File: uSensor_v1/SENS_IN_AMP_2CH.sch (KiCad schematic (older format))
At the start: 19 parts, among them U16 TBD

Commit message: Layout correction in progress.
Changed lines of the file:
@@
 AR Path="/5CFE311F/5C6F0205" Ref="R52"  Part="1"
 AR Path="/5E594B34/5C6F0205" Ref="R60"  Part="1"
-F 0 "R52" V 2443 3950 50  0000 C CNN
+F 0 "R60" V 2443 3950 50  0000 C CNN
 F 1 "10k 1%" V 2534 3950 50  0000 C CNN
 F 2 "Resistor_SMD:R_0603_1608Metric_Pad1.05x0.95mm_HandSolder" V 2580 3950 50  0001 C CNN
@@
 AR Path="/5CFE311F/5C6F020C" Ref="C49"  Part="1"
 AR Path="/5E594B34/5C6F020C" Ref="C53"  Part="1"
-F 0 "C49" V 3298 2800 50  0000 C CNN
+F 0 "C53" V 3298 2800 50  0000 C CNN
 F 1 "1p 16V X5R" V 3389 2800 50  0000 C CNN
 F 2 "Capacitor_SMD:C_0603_1608Metric_Pad1.05x0.95mm_HandSolder" H 3588 2650 50  0001 C CNN
@@
 AR Path="/5CFE311F/5C6F0213" Ref="R54"  Part="1"
 AR Path="/5E594B34/5C6F0213" Ref="R62"  Part="1"
-F 0 "R54" H 2830 4154 50  0000 R CNN
+F 0 "R62" H 2830 4154 50  0000 R CNN
 F 1 "22k 1%" H 2830 4245 50  0000 R CNN
 F 2 "Resistor_SMD:R_0603_1608Metric_Pad1.05x0.95mm_HandSolder" V 2830 4200 50  0001 C CNN
@@
 AR Path="/5CFE311F/5C6F0221" Ref="R36"  Part="1"
 AR Path="/5E594B34/5C6F0221" Ref="R58"  Part="1"
-F 0 "R36" V 2443 3600 50  0000 C CNN
+F 0 "R58" V 2443 3600 50  0000 C CNN
 F 1 "10k 1%" V 2534 3600 50  0000 C CNN
 F 2 "Resistor_SMD:R_0603_1608Metric_Pad1.05x0.95mm_HandSolder" V 2580 3600 50  0001 C CNN
@@
 AR Path="/5CFE311F/5C6F0228" Ref="R34"  Part="1"
 AR Path="/5E594B34/5C6F0228" Ref="R56"  Part="1"
-F 0 "R34" V 3343 3150 50  0000 C CNN
+F 0 "R56" V 3343 3150 50  0000 C CNN
 F 1 "22k 1%" V 3434 3150 50  0000 C CNN
 F 2 "Resistor_SMD:R_0603_1608Metric_Pad1.05x0.95mm_HandSolder" V 3480 3150 50  0001 C CNN
@@
 AR Path="/5CFE311F/5D2C6388" Ref="TP61"  Part="1"
 AR Path="/5E594B34/5D2C6388" Ref="TP65"  Part="1"
-F 0 "TP61" H 3100 3225 50  0000 C CNN
+F 0 "TP65" H 3100 3225 50  0000 C CNN
 F 1 "TP" H 3100 3134 50  0000 C CNN
 F 2 "Sentisa-Connectors:TestPoint_Probe_1.0mmDiameter_0.6mmDrill" H 3300 2900 50  0001 C CNN
@@
 AR Path="/5CFE311F/5D2C69C6" Ref="TP63"  Part="1"
 AR Path="/5E594B34/5D2C69C6" Ref="TP67"  Part="1"
-F 0 "TP63" H 3200 3975 50  0000 C CNN
+F 0 "TP67" H 3200 3975 50  0000 C CNN
 F 1 "TP" H 3200 3884 50  0000 C CNN
 F 2 "Sentisa-Connectors:TestPoint_Probe_1.0mmDiameter_0.6mmDrill" H 3400 3650 50  0001 C CNN
@@
 AR Path="/5CFE311F/5D1D3C08" Ref="R53"  Part="1"
 AR Path="/5E594B34/5D1D3C08" Ref="R61"  Part="1"
-F 0 "R53" V 5743 3950 50  0000 C CNN
+F 0 "R61" V 5743 3950 50  0000 C CNN
 F 1 "10k 1%" V 5834 3950 50  0000 C CNN
 F 2 "Resistor_SMD:R_0603_1608Metric_Pad1.05x0.95mm_HandSolder" V 5880 3950 50  0001 C CNN
@@
 AR Path="/5CFE311F/5D1D3C0F" Ref="C50"  Part="1"
 AR Path="/5E594B34/5D1D3C0F" Ref="C55"  Part="1"
-F 0 "C50" V 6598 2800 50  0000 C CNN
+F 0 "C55" V 6598 2800 50  0000 C CNN
 F 1 "1p 16V X5R" V 6689 2800 50  0000 C CNN
 F 2 "Capacitor_SMD:C_0603_1608Metric_Pad1.05x0.95mm_HandSolder" H 6888 2650 50  0001 C CNN
@@
 AR Path="/5CFE311F/5D1D3C16" Ref="R55"  Part="1"
 AR Path="/5E594B34/5D1D3C16" Ref="R63"  Part="1"
-F 0 "R55" H 6130 4154 50  0000 R CNN
+F 0 "R63" H 6130 4154 50  0000 R CNN
 F 1 "22k 1%" H 6130 4245 50  0000 R CNN
 F 2 "Resistor_SMD:R_0603_1608Metric_Pad1.05x0.95mm_HandSolder" V 6130 4200 50  0001 C CNN
@@
 AR Path="/5CFE311F/5D1D3C22" Ref="R37"  Part="1"
 AR Path="/5E594B34/5D1D3C22" Ref="R59"  Part="1"
-F 0 "R37" V 5743 3600 50  0000 C CNN
+F 0 "R59" V 5743 3600 50  0000 C CNN
 F 1 "10k 1%" V 5834 3600 50  0000 C CNN
 F 2 "Resistor_SMD:R_0603_1608Metric_Pad1.05x0.95mm_HandSolder" V 5880 3600 50  0001 C CNN
@@
 AR Path="/5CFE311F/5D1D3C29" Ref="R35"  Part="1"
 AR Path="/5E594B34/5D1D3C29" Ref="R57"  Part="1"
-F 0 "R35" V 6643 3150 50  0000 C CNN
+F 0 "R57" V 6643 3150 50  0000 C CNN
 F 1 "22k 1%" V 6734 3150 50  0000 C CNN
 F 2 "Resistor_SMD:R_0603_1608Metric_Pad1.05x0.95mm_HandSolder" V 6780 3150 50  0001 C CNN
@@
 AR Path="/5CFE311F/5D1D3C38" Ref="C51"  Part="1"
 AR Path="/5E594B34/5D1D3C38" Ref="C56"  Part="1"
-F 0 "C51" H 9215 3296 50  0000 L CNN
+F 0 "C56" H 9215 3296 50  0000 L CNN
 F 1 "100n 6V3 X5R" H 9215 3205 50  0000 L CNN
 F 2 "Capacitor_SMD:C_0603_1608Metric_Pad1.05x0.95mm_HandSolder" H 9138 3100 50  0001 C CNN
@@
 AR Path="/5CFE311F/5D1D3C3F" Ref="C52"  Part="1"
 AR Path="/5E594B34/5D1D3C3F" Ref="C58"  Part="1"
-F 0 "C52" H 9215 4546 50  0000 L CNN
+F 0 "C58" H 9215 4546 50  0000 L CNN
 F 1 "100n 6V3 X5R" H 9215 4455 50  0000 L CNN
 F 2 "Capacitor_SMD:C_0603_1608Metric_Pad1.05x0.95mm_HandSolder" H 9138 4350 50  0001 C CNN
@@
 AR Path="/5CFE311F/5D1D3C6C" Ref="TP62"  Part="1"
 AR Path="/5E594B34/5D1D3C6C" Ref="TP66"  Part="1"
-F 0 "TP62" H 6400 3225 50  0000 C CNN
+F 0 "TP66" H 6400 3225 50  0000 C CNN
 F 1 "TP" H 6400 3134 50  0000 C CNN
 F 2 "Sentisa-Connectors:TestPoint_Probe_1.0mmDiameter_0.6mmDrill" H 6600 2900 50  0001 C CNN
@@
 AR Path="/5CFE311F/5D1D3C73" Ref="TP64"  Part="1"
 AR Path="/5E594B34/5D1D3C73" Ref="TP68"  Part="1"
-F 0 "TP64" H 6500 3975 50  0000 C CNN
+F 0 "TP68" H 6500 3975 50  0000 C CNN
 F 1 "TP" H 6500 3884 50  0000 C CNN
 F 2 "Sentisa-Connectors:TestPoint_Probe_1.0mmDiameter_0.6mmDrill" H 6700 3650 50  0001 C CNN
@@
 AR Path="/5CFE311F/5F717FB4" Ref="U16"  Part="1"
 AR Path="/5E594B34/5F717FB4" Ref="U17"  Part="1"
-F 0 "U16" H 3600 4217 50  0000 C CNN
+F 0 "U17" H 3600 4217 50  0000 C CNN
 F 1 "TBD" H 3600 4126 50  0000 C CNN
 F 2 "Sentisa-IC:SO-8" H 3600 3850 50  0001 C CNN
@@
 AR Path="/5CFE311F/5F718017" Ref="U16"  Part="2"
 AR Path="/5E594B34/5F718017" Ref="U17"  Part="2"
-F 0 "U16" H 6900 4217 50  0000 C CNN
+F 0 "U17" H 6900 4217 50  0000 C CNN
 F 1 "TBD" H 6900 4126 50  0000 C CNN
 F 2 "Sentisa-IC:SO-8" H 6900 3850 50  0001 C CNN
@@
 AR Path="/5CFE311F/5F7180AE" Ref="U16"  Part="3"
 AR Path="/5E594B34/5F7180AE" Ref="U17"  Part="3"
-F 0 "U16" H 8808 3646 50  0000 L CNN
+F 0 "U17" H 8808 3646 50  0000 L CNN
 F 1 "TBD" H 8808 3555 50  0000 L CNN
 F 2 "Sentisa-IC:SO-8" H 8850 3600 50  0001 C CNN
@@
 AR Path="/5E594B34/5D0CECC5" Ref="C60"  Part="1"
 AR Path="/5CFE311F/5D0CECC5" Ref="C48"  Part="1"
-F 0 "C48" H 5585 4246 50  0000 R CNN
+F 0 "C60" H 5585 4246 50  0000 R CNN
 F 1 "10n 6V3 X5R" H 5585 4155 50  0000 R CNN
 F 2 "Capacitor_SMD:C_0603_1608Metric_Pad1.05x0.95mm_HandSolder" H 5738 4050 50  0001 C CNN
@@
 AR Path="/5E594B34/5D0D3A39" Ref="C59"  Part="1"
 AR Path="/5CFE311F/5D0D3A39" Ref="C44"  Part="1"
-F 0 "C44" H 2285 4246 50  0000 R CNN
+F 0 "C59" H 2285 4246 50  0000 R CNN
 F 1 "10n 6V3 X5R" H 2285 4155 50  0000 R CNN
 F 2 "Capacitor_SMD:C_0603_1608Metric_Pad1.05x0.95mm_HandSolder" H 2438 4050 50  0001 C CNN

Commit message: Components checked.
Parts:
- U16: value TBD -> MCP6H02-E/SN; MFR TBD -> Microchip; MPN TBD -> MCP6H02-E/SN
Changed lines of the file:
@@
 AR Path="/5CFE311F/5C6F0205" Ref="R52"  Part="1"
 AR Path="/5E594B34/5C6F0205" Ref="R60"  Part="1"
-F 0 "R60" V 2443 3950 50  0000 C CNN
+F 0 "R52" V 2443 3950 50  0000 C CNN
 F 1 "10k 1%" V 2534 3950 50  0000 C CNN
 F 2 "Resistor_SMD:R_0603_1608Metric_Pad1.05x0.95mm_HandSolder" V 2580 3950 50  0001 C CNN
@@
 AR Path="/5CFE311F/5C6F020C" Ref="C49"  Part="1"
 AR Path="/5E594B34/5C6F020C" Ref="C53"  Part="1"
-F 0 "C53" V 3298 2800 50  0000 C CNN
+F 0 "C49" V 3298 2800 50  0000 C CNN
 F 1 "1p 16V X5R" V 3389 2800 50  0000 C CNN
 F 2 "Capacitor_SMD:C_0603_1608Metric_Pad1.05x0.95mm_HandSolder" H 3588 2650 50  0001 C CNN
@@
 AR Path="/5CFE311F/5C6F0213" Ref="R54"  Part="1"
 AR Path="/5E594B34/5C6F0213" Ref="R62"  Part="1"
-F 0 "R62" H 2830 4154 50  0000 R CNN
+F 0 "R54" H 2830 4154 50  0000 R CNN
 F 1 "22k 1%" H 2830 4245 50  0000 R CNN
 F 2 "Resistor_SMD:R_0603_1608Metric_Pad1.05x0.95mm_HandSolder" V 2830 4200 50  0001 C CNN
@@
 AR Path="/5CFE311F/5C6F0221" Ref="R36"  Part="1"
 AR Path="/5E594B34/5C6F0221" Ref="R58"  Part="1"
-F 0 "R58" V 2443 3600 50  0000 C CNN
+F 0 "R36" V 2443 3600 50  0000 C CNN
 F 1 "10k 1%" V 2534 3600 50  0000 C CNN
 F 2 "Resistor_SMD:R_0603_1608Metric_Pad1.05x0.95mm_HandSolder" V 2580 3600 50  0001 C CNN
@@
 AR Path="/5CFE311F/5C6F0228" Ref="R34"  Part="1"
 AR Path="/5E594B34/5C6F0228" Ref="R56"  Part="1"
-F 0 "R56" V 3343 3150 50  0000 C CNN
+F 0 "R34" V 3343 3150 50  0000 C CNN
 F 1 "22k 1%" V 3434 3150 50  0000 C CNN
 F 2 "Resistor_SMD:R_0603_1608Metric_Pad1.05x0.95mm_HandSolder" V 3480 3150 50  0001 C CNN
@@
 AR Path="/5CFE311F/5D2C6388" Ref="TP61"  Part="1"
 AR Path="/5E594B34/5D2C6388" Ref="TP65"  Part="1"
-F 0 "TP65" H 3100 3225 50  0000 C CNN
+F 0 "TP61" H 3100 3225 50  0000 C CNN
 F 1 "TP" H 3100 3134 50  0000 C CNN
 F 2 "Sentisa-Connectors:TestPoint_Probe_1.0mmDiameter_0.6mmDrill" H 3300 2900 50  0001 C CNN
@@
 AR Path="/5CFE311F/5D2C69C6" Ref="TP63"  Part="1"
 AR Path="/5E594B34/5D2C69C6" Ref="TP67"  Part="1"
-F 0 "TP67" H 3200 3975 50  0000 C CNN
+F 0 "TP63" H 3200 3975 50  0000 C CNN
 F 1 "TP" H 3200 3884 50  0000 C CNN
 F 2 "Sentisa-Connectors:TestPoint_Probe_1.0mmDiameter_0.6mmDrill" H 3400 3650 50  0001 C CNN
@@
 AR Path="/5CFE311F/5D1D3C08" Ref="R53"  Part="1"
 AR Path="/5E594B34/5D1D3C08" Ref="R61"  Part="1"
-F 0 "R61" V 5743 3950 50  0000 C CNN
+F 0 "R53" V 5743 3950 50  0000 C CNN
 F 1 "10k 1%" V 5834 3950 50  0000 C CNN
 F 2 "Resistor_SMD:R_0603_1608Metric_Pad1.05x0.95mm_HandSolder" V 5880 3950 50  0001 C CNN
@@
 AR Path="/5CFE311F/5D1D3C0F" Ref="C50"  Part="1"
 AR Path="/5E594B34/5D1D3C0F" Ref="C55"  Part="1"
-F 0 "C55" V 6598 2800 50  0000 C CNN
+F 0 "C50" V 6598 2800 50  0000 C CNN
 F 1 "1p 16V X5R" V 6689 2800 50  0000 C CNN
 F 2 "Capacitor_SMD:C_0603_1608Metric_Pad1.05x0.95mm_HandSolder" H 6888 2650 50  0001 C CNN
@@
 AR Path="/5CFE311F/5D1D3C16" Ref="R55"  Part="1"
 AR Path="/5E594B34/5D1D3C16" Ref="R63"  Part="1"
-F 0 "R63" H 6130 4154 50  0000 R CNN
+F 0 "R55" H 6130 4154 50  0000 R CNN
 F 1 "22k 1%" H 6130 4245 50  0000 R CNN
 F 2 "Resistor_SMD:R_0603_1608Metric_Pad1.05x0.95mm_HandSolder" V 6130 4200 50  0001 C CNN
@@
 AR Path="/5CFE311F/5D1D3C22" Ref="R37"  Part="1"
 AR Path="/5E594B34/5D1D3C22" Ref="R59"  Part="1"
-F 0 "R59" V 5743 3600 50  0000 C CNN
+F 0 "R37" V 5743 3600 50  0000 C CNN
 F 1 "10k 1%" V 5834 3600 50  0000 C CNN
 F 2 "Resistor_SMD:R_0603_1608Metric_Pad1.05x0.95mm_HandSolder" V 5880 3600 50  0001 C CNN
@@
 AR Path="/5CFE311F/5D1D3C29" Ref="R35"  Part="1"
 AR Path="/5E594B34/5D1D3C29" Ref="R57"  Part="1"
-F 0 "R57" V 6643 3150 50  0000 C CNN
+F 0 "R35" V 6643 3150 50  0000 C CNN
 F 1 "22k 1%" V 6734 3150 50  0000 C CNN
 F 2 "Resistor_SMD:R_0603_1608Metric_Pad1.05x0.95mm_HandSolder" V 6780 3150 50  0001 C CNN
@@
 AR Path="/5CFE311F/5D1D3C38" Ref="C51"  Part="1"
 AR Path="/5E594B34/5D1D3C38" Ref="C56"  Part="1"
-F 0 "C56" H 9215 3296 50  0000 L CNN
+F 0 "C51" H 9215 3296 50  0000 L CNN
 F 1 "100n 6V3 X5R" H 9215 3205 50  0000 L CNN
 F 2 "Capacitor_SMD:C_0603_1608Metric_Pad1.05x0.95mm_HandSolder" H 9138 3100 50  0001 C CNN
@@
 AR Path="/5CFE311F/5D1D3C3F" Ref="C52"  Part="1"
 AR Path="/5E594B34/5D1D3C3F" Ref="C58"  Part="1"
-F 0 "C58" H 9215 4546 50  0000 L CNN
+F 0 "C52" H 9215 4546 50  0000 L CNN
 F 1 "100n 6V3 X5R" H 9215 4455 50  0000 L CNN
 F 2 "Capacitor_SMD:C_0603_1608Metric_Pad1.05x0.95mm_HandSolder" H 9138 4350 50  0001 C CNN
@@
 AR Path="/5CFE311F/5D1D3C6C" Ref="TP62"  Part="1"
 AR Path="/5E594B34/5D1D3C6C" Ref="TP66"  Part="1"
-F 0 "TP66" H 6400 3225 50  0000 C CNN
+F 0 "TP62" H 6400 3225 50  0000 C CNN
 F 1 "TP" H 6400 3134 50  0000 C CNN
 F 2 "Sentisa-Connectors:TestPoint_Probe_1.0mmDiameter_0.6mmDrill" H 6600 2900 50  0001 C CNN
@@
 AR Path="/5CFE311F/5D1D3C73" Ref="TP64"  Part="1"
 AR Path="/5E594B34/5D1D3C73" Ref="TP68"  Part="1"
-F 0 "TP68" H 6500 3975 50  0000 C CNN
+F 0 "TP64" H 6500 3975 50  0000 C CNN
 F 1 "TP" H 6500 3884 50  0000 C CNN
 F 2 "Sentisa-Connectors:TestPoint_Probe_1.0mmDiameter_0.6mmDrill" H 6700 3650 50  0001 C CNN
@@
 AR Path="/5CFE311F/5F717FB4" Ref="U16"  Part="1"
 AR Path="/5E594B34/5F717FB4" Ref="U17"  Part="1"
-F 0 "U17" H 3600 4217 50  0000 C CNN
-F 1 "TBD" H 3600 4126 50  0000 C CNN
+F 0 "U16" H 3600 4217 50  0000 C CNN
+F 1 "MCP6H02-E/SN" H 3600 4126 50  0000 C CNN
 F 2 "Sentisa-IC:SO-8" H 3600 3850 50  0001 C CNN
 F 3 "" H 3600 3850 50  0001 C CNN
-F 4 "TBD" H 3600 3850 50  0001 C CNN "MFR"
-F 5 "TBD" H 3600 3850 50  0001 C CNN "MPN"
+F 4 "Microchip" H 3600 3850 50  0001 C CNN "MFR"
+F 5 "MCP6H02-E/SN" H 3600 3850 50  0001 C CNN "MPN"
 	1    3600 3850
 	1    0    0    -1
@@
 AR Path="/5CFE311F/5F718017" Ref="U16"  Part="2"
 AR Path="/5E594B34/5F718017" Ref="U17"  Part="2"
-F 0 "U17" H 6900 4217 50  0000 C CNN
-F 1 "TBD" H 6900 4126 50  0000 C CNN
+F 0 "U16" H 6900 4217 50  0000 C CNN
+F 1 "MCP6H02-E/SN" H 6900 4126 50  0000 C CNN
 F 2 "Sentisa-IC:SO-8" H 6900 3850 50  0001 C CNN
 F 3 "" H 6900 3850 50  0001 C CNN
-F 4 "TBD" H 6900 3850 50  0001 C CNN "MFR"
-F 5 "TBD" H 6900 3850 50  0001 C CNN "MPN"
+F 4 "Microchip" H 6900 3850 50  0001 C CNN "MFR"
+F 5 "MCP6H02-E/SN" H 6900 3850 50  0001 C CNN "MPN"
 	2    6900 3850
 	1    0    0    -1
@@
 AR Path="/5CFE311F/5F7180AE" Ref="U16"  Part="3"
 AR Path="/5E594B34/5F7180AE" Ref="U17"  Part="3"
-F 0 "U17" H 8808 3646 50  0000 L CNN
+F 0 "U16" H 8808 3646 50  0000 L CNN
 F 1 "TBD" H 8808 3555 50  0000 L CNN
 F 2 "Sentisa-IC:SO-8" H 8850 3600 50  0001 C CNN
@@
 AR Path="/5E594B34/5D0CECC5" Ref="C60"  Part="1"
 AR Path="/5CFE311F/5D0CECC5" Ref="C48"  Part="1"
-F 0 "C60" H 5585 4246 50  0000 R CNN
+F 0 "C48" H 5585 4246 50  0000 R CNN
 F 1 "10n 6V3 X5R" H 5585 4155 50  0000 R CNN
 F 2 "Capacitor_SMD:C_0603_1608Metric_Pad1.05x0.95mm_HandSolder" H 5738 4050 50  0001 C CNN
@@
 AR Path="/5E594B34/5D0D3A39" Ref="C59"  Part="1"
 AR Path="/5CFE311F/5D0D3A39" Ref="C44"  Part="1"
-F 0 "C59" H 2285 4246 50  0000 R CNN
+F 0 "C44" H 2285 4246 50  0000 R CNN
 F 1 "10n 6V3 X5R" H 2285 4155 50  0000 R CNN
 F 2 "Capacitor_SMD:C_0603_1608Metric_Pad1.05x0.95mm_HandSolder" H 2438 4050 50  0001 C CNN

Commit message: Layout in progress (adding vias)
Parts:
- U16: value TBD -> MCP6H02-E/SN; MFR TBD -> Microchip; MPN TBD -> MCP6H02-E/SN
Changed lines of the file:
@@
 AR Path="/5E594B34/5F7180AE" Ref="U17"  Part="3"
 F 0 "U16" H 8808 3646 50  0000 L CNN
-F 1 "TBD" H 8808 3555 50  0000 L CNN
+F 1 "MCP6H02-E/SN" H 8808 3555 50  0000 L CNN
 F 2 "Sentisa-IC:SO-8" H 8850 3600 50  0001 C CNN
 F 3 "" H 8850 3600 50  0001 C CNN
-F 4 "TBD" H 8850 3600 50  0001 C CNN "MFR"
-F 5 "TBD" H 8850 3600 50  0001 C CNN "MPN"
+F 4 "Microchip" H 8850 3600 50  0001 C CNN "MFR"
+F 5 "MCP6H02-E/SN" H 8850 3600 50  0001 C CNN "MPN"
 	3    8850 3600
 	1    0    0    -1

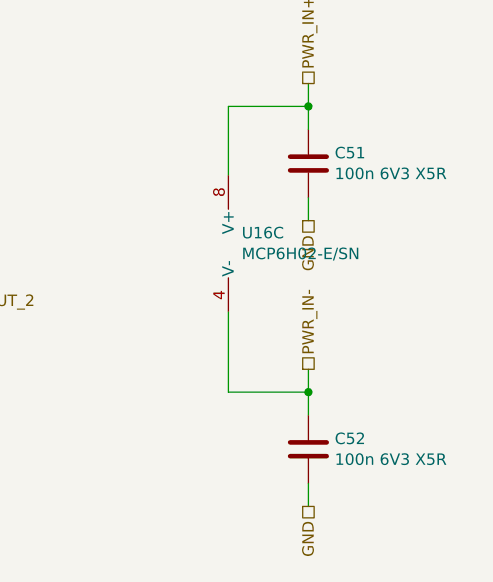
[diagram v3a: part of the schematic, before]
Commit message: Unificated some components. Order ready.
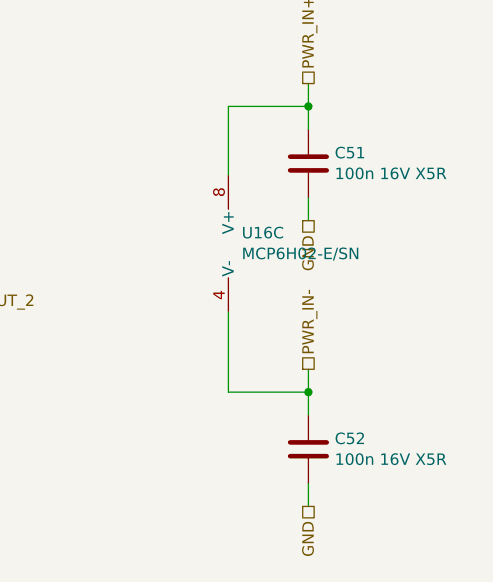
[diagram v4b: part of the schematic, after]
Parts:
- C51, C52: value 100n 6V3 X5R -> 100n 16V X5R
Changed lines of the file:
@@
 AR Path="/5E594B34/5D1D3C38" Ref="C56"  Part="1"
 F 0 "C51" H 9215 3296 50  0000 L CNN
-F 1 "100n 6V3 X5R" H 9215 3205 50  0000 L CNN
+F 1 "100n 16V X5R" H 9215 3205 50  0000 L CNN
 F 2 "Capacitor_SMD:C_0603_1608Metric_Pad1.05x0.95mm_HandSolder" H 9138 3100 50  0001 C CNN
 F 3 "~" H 9100 3250 50  0001 C CNN
@@
 AR Path="/5E594B34/5D1D3C3F" Ref="C58"  Part="1"
 F 0 "C52" H 9215 4546 50  0000 L CNN
-F 1 "100n 6V3 X5R" H 9215 4455 50  0000 L CNN
+F 1 "100n 16V X5R" H 9215 4455 50  0000 L CNN
 F 2 "Capacitor_SMD:C_0603_1608Metric_Pad1.05x0.95mm_HandSolder" H 9138 4350 50  0001 C CNN
 F 3 "~" H 9100 4500 50  0001 C CNN
